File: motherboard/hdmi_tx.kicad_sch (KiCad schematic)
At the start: 49 parts, among them J8 HDMI_A, Q1 2SK3018W, Q2 2SK3018W, Q3 L2N7002WT1G, Q4 2SK3018W, Q5 2SK3018W, Q6 WNM6002-3/TR, Q7 WNM6002-3/TR, Q8 WNM6002-3/TR, Q9 WNM6002-3/TR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

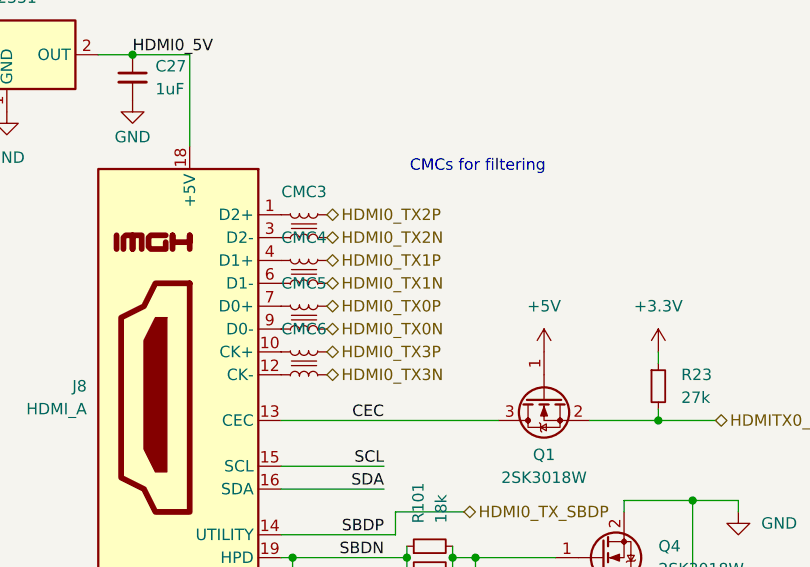
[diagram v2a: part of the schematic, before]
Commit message: 6 layer for better high speed signaling integrity
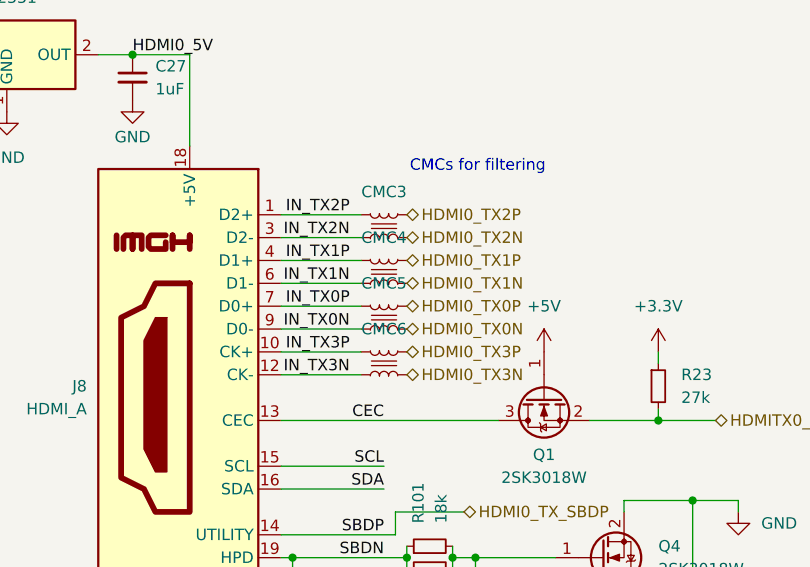
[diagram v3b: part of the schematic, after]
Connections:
- net IN_TX0N: now reaches CMC5.1, J8.9 (D0-)
- net IN_TX0P: now reaches CMC5.2, J8.7 (D0+)
- net IN_TX2P: now reaches CMC3.2, J8.1 (D2+)
- net IN_TX3P: now reaches CMC6.2, J8.10 (CK+)
- net IN_TX3N: now reaches CMC6.1, J8.12 (CK-)
- net IN_TX2N: now reaches CMC3.1, J8.3 (D2-)
- net IN_TX1P: now reaches CMC4.2, J8.4 (D1+)
- net IN_TX1N: now reaches CMC4.1, J8.6 (D1-)
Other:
- moved on the sheet: CMC3, CMC4, CMC5, CMC6
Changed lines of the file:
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@@
 	(wire
 		(pts
+			(xy 73.66 73.66) (xy 64.77 73.66)
+		)
+		(stroke
+			(width 0)
+			(type default)
+		)
+	)
+	(wire
+		(pts
+			(xy 73.66 76.2) (xy 64.77 76.2)
+		)
+		(stroke
+			(width 0)
+			(type default)
+		)
+	)
+	(wire
+		(pts
 			(xy 264.16 110.49) (xy 264.16 125.73)
 		)
@@
 	(wire
 		(pts
+			(xy 73.66 68.58) (xy 64.77 68.58)
+		)
+		(stroke
+			(width 0)
+			(type default)
+		)
+	)
+	(wire
+		(pts
+			(xy 73.66 63.5) (xy 64.77 63.5)
+		)
+		(stroke
+			(width 0)
+			(type default)
+		)
+	)
+	(wire
+		(pts
 			(xy 76.2 168.91) (xy 67.31 168.91)
 		)
@@
 	(wire
 		(pts
+			(xy 73.66 58.42) (xy 64.77 58.42)
+		)
+		(stroke
+			(width 0)
+			(type default)
+		)
+	)
+	(wire
+		(pts
 			(xy 207.01 49.53) (xy 207.01 50.8)
 		)
@@
 	(wire
 		(pts
+			(xy 73.66 66.04) (xy 64.77 66.04)
+		)
+		(stroke
+			(width 0)
+			(type default)
+		)
+	)
+	(wire
+		(pts
 			(xy 233.68 118.11) (xy 233.68 125.73)
 		)
@@
 	(wire
 		(pts
+			(xy 73.66 71.12) (xy 64.77 71.12)
+		)
+		(stroke
+			(width 0)
+			(type default)
+		)
+	)
+	(wire
+		(pts
 			(xy 267.97 134.62) (xy 267.97 132.08)
 		)
@@
 	(wire
 		(pts
+			(xy 73.66 60.96) (xy 64.77 60.96)
+		)
+		(stroke
+			(width 0)
+			(type default)
+		)
+	)
+	(wire
+		(pts
 			(xy 264.16 110.49) (xy 266.7 110.49)
 		)
@@
 		)
 	)
+	(label "IN_TX1P"
+		(at 72.39 63.5 180)
+		(fields_autoplaced yes)
+		(effects
+			(font
+				(size 1.27 1.27)
+			)
+			(justify right bottom)
+		)
+	)
 	(label "SBDN"
 		(at 110.49 173.99 180)
@@
 		)
 	)
+	(label "IN_TX1N"
+		(at 72.39 66.04 180)
+		(fields_autoplaced yes)
+		(effects
+			(font
+				(size 1.27 1.27)
+			)
+			(justify right bottom)
+		)
+	)
 	(label "SBDP"
 		(at 67.31 179.07 0)
@@
 		)
 	)
+	(label "IN_TX0N"
+		(at 72.39 71.12 180)
+		(fields_autoplaced yes)
+		(effects
+			(font
+				(size 1.27 1.27)
+			)
+			(justify right bottom)
+		)
+	)
 	(label "HDMI0_TX3N"
 		(at 156.21 149.86 180)
@@
 		)
 	)
+	(label "IN_TX3N"
+		(at 72.39 76.2 180)
+		(fields_autoplaced yes)
+		(effects
+			(font
+				(size 1.27 1.27)
+			)
+			(justify right bottom)
+		)
+	)
 	(label "HDMI0_TX2N"
 		(at 19.05 149.86 0)
@@
 		)
 	)
+	(label "IN_TX3P"
+		(at 72.39 73.66 180)
+		(fields_autoplaced yes)
+		(effects
+			(font
+				(size 1.27 1.27)
+			)
+			(justify right bottom)
+		)
+	)
 	(label "HDMI0_TX3P"
 		(at 181.61 123.19 0)
@@
 		)
 	)
+	(label "IN_TX2P"
+		(at 72.39 58.42 180)
+		(fields_autoplaced yes)
+		(effects
+			(font
+				(size 1.27 1.27)
+			)
+			(justify right bottom)
+		)
+	)
 	(label "HDMI0_TX2P"
 		(at 19.05 139.7 0)
@@
 		)
 	)
+	(label "IN_TX2N"
+		(at 72.39 60.96 180)
+		(fields_autoplaced yes)
+		(effects
+			(font
+				(size 1.27 1.27)
+			)
+			(justify right bottom)
+		)
+	)
+	(label "IN_TX0P"
+		(at 72.39 68.58 180)
+		(fields_autoplaced yes)
+		(effects
+			(font
+				(size 1.27 1.27)
+			)
+			(justify right bottom)
+		)
+	)
 	(label "HDMI0_TX1N"
 		(at 88.9 154.94 180)
@@
 	(hierarchical_label "HDMI0_TX1P"
 		(shape bidirectional)
-		(at 69.85 63.5 0)
+		(at 78.74 63.5 0)
 		(fields_autoplaced yes)
 		(effects
@@
 	(hierarchical_label "HDMI0_TX0N"
 		(shape bidirectional)
-		(at 69.85 71.12 0)
+		(at 78.74 71.12 0)
 		(fields_autoplaced yes)
 		(effects
@@
 	(hierarchical_label "HDMI0_TX0P"
 		(shape bidirectional)
-		(at 69.85 68.58 0)
+		(at 78.74 68.58 0)
 		(fields_autoplaced yes)
 		(effects
@@
 	(hierarchical_label "HDMI0_TX2N"
 		(shape bidirectional)
-		(at 69.85 60.96 0)
+		(at 78.74 60.96 0)
 		(fields_autoplaced yes)
 		(effects
@@
 	(hierarchical_label "HDMI0_TX3P"
 		(shape bidirectional)
-		(at 69.85 73.66 0)
+		(at 78.74 73.66 0)
 		(fields_autoplaced yes)
 		(effects
@@
 	(hierarchical_label "HDMI0_TX2P"
 		(shape bidirectional)
-		(at 69.85 58.42 0)
+		(at 78.74 58.42 0)
 		(fields_autoplaced yes)
 		(effects
@@
 	(hierarchical_label "HDMI0_TX3N"
 		(shape bidirectional)
-		(at 69.85 76.2 0)
+		(at 78.74 76.2 0)
 		(fields_autoplaced yes)
 		(effects
@@
 	(hierarchical_label "HDMI0_TX1N"
 		(shape bidirectional)
-		(at 69.85 66.04 0)
+		(at 78.74 66.04 0)
 		(fields_autoplaced yes)
 		(effects
@@
 	(symbol
 		(lib_id "library:ACM2012_Common_Mode_Choke")
-		(at 67.31 69.85 0)
+		(at 76.2 69.85 0)
 		(unit 1)
 		(exclude_from_sim no)
@@
 		(fields_autoplaced yes)
 		(property "Reference" "CMC5"
-			(at 67.31 66.04 0)
+			(at 76.2 66.04 0)
 			(effects
 				(font
@@
 		)
 		(property "Value" "ACM2012"
-			(at 71.501 73.025 0)
+			(at 80.391 73.025 0)
 			(effects
 				(font
@@
 		)
 		(property "Footprint" "ACM2012:FIL_ACM2012-900-2P-T001"
-			(at 65.278 78.232 0)
+			(at 74.168 78.232 0)
 			(effects
 				(font
@@
 		)
 		(property "Datasheet" "https://product.tdk.com/en/system/files?file=dam/doc/product/emc/emc/cmf_cmc/catalog/cmf_commercial_signal_acm2012_en.pdf"
-			(at 69.342 81.788 0)
+			(at 78.232 81.788 0)
 			(effects
 				(font
@@
 		)
 		(property "Description" "2 Line Common Mode Choke Surface Mount 90 Ohms @ 100 MHz 400mA DCR 190mOhm"
-			(at 67.818 75.946 0)
+			(at 76.708 75.946 0)
 			(effects
 				(font
@@
 	(symbol
 		(lib_id "library:ACM2012_Common_Mode_Choke")
-		(at 67.31 74.93 0)
+		(at 76.2 74.93 0)
 		(unit 1)
 		(exclude_from_sim no)
@@
 		(fields_autoplaced yes)
 		(property "Reference" "CMC6"
-			(at 67.31 71.12 0)
+			(at 76.2 71.12 0)
 			(effects
 				(font
@@
 		)
 		(property "Value" "ACM2012"
-			(at 71.501 78.105 0)
+			(at 80.391 78.105 0)
 			(effects
 				(font
@@
 		)
 		(property "Footprint" "ACM2012:FIL_ACM2012-900-2P-T001"
-			(at 65.278 83.312 0)
+			(at 74.168 83.312 0)
 			(effects
 				(font
@@
 		)
 		(property "Datasheet" "https://product.tdk.com/en/system/files?file=dam/doc/product/emc/emc/cmf_cmc/catalog/cmf_commercial_signal_acm2012_en.pdf"
-			(at 69.342 86.868 0)
+			(at 78.232 86.868 0)
 			(effects
 				(font
@@
 		)
 		(property "Description" "2 Line Common Mode Choke Surface Mount 90 Ohms @ 100 MHz 400mA DCR 190mOhm"
-			(at 67.818 81.026 0)
+			(at 76.708 81.026 0)
 			(effects
 				(font
@@
 	(symbol
 		(lib_id "library:ACM2012_Common_Mode_Choke")
-		(at 67.31 64.77 0)
+		(at 76.2 64.77 0)
 		(unit 1)
 		(exclude_from_sim no)
@@
 		(fields_autoplaced yes)
 		(property "Reference" "CMC4"
-			(at 67.31 60.96 0)
+			(at 76.2 60.96 0)
 			(effects
 				(font
@@
 		)
 		(property "Value" "ACM2012"
-			(at 71.501 67.945 0)
+			(at 80.391 67.945 0)
 			(effects
 				(font
@@
 		)
 		(property "Footprint" "ACM2012:FIL_ACM2012-900-2P-T001"
-			(at 65.278 73.152 0)
+			(at 74.168 73.152 0)
 			(effects
 				(font
@@
 		)
 		(property "Datasheet" "https://product.tdk.com/en/system/files?file=dam/doc/product/emc/emc/cmf_cmc/catalog/cmf_commercial_signal_acm2012_en.pdf"
-			(at 69.342 76.708 0)
+			(at 78.232 76.708 0)
 			(effects
 				(font
@@
 		)
 		(property "Description" "2 Line Common Mode Choke Surface Mount 90 Ohms @ 100 MHz 400mA DCR 190mOhm"
-			(at 67.818 70.866 0)
+			(at 76.708 70.866 0)
 			(effects
 				(font
@@
 	(symbol
 		(lib_id "library:ACM2012_Common_Mode_Choke")
-		(at 67.31 59.69 0)
+		(at 76.2 59.69 0)
 		(unit 1)
 		(exclude_from_sim no)
@@
 		(fields_autoplaced yes)
 		(property "Reference" "CMC3"
-			(at 67.31 55.88 0)
+			(at 76.2 55.88 0)
 			(effects
 				(font
@@
 		)
 		(property "Value" "ACM2012"
-			(at 71.501 62.865 0)
+			(at 80.391 62.865 0)
 			(effects
 				(font
@@
 		)
 		(property "Footprint" "ACM2012:FIL_ACM2012-900-2P-T001"
-			(at 65.278 68.072 0)
+			(at 74.168 68.072 0)
 			(effects
 				(font
@@
 		)
 		(property "Datasheet" "https://product.tdk.com/en/system/files?file=dam/doc/product/emc/emc/cmf_cmc/catalog/cmf_commercial_signal_acm2012_en.pdf"
-			(at 69.342 71.628 0)
+			(at 78.232 71.628 0)
 			(effects
 				(font
@@
 		)
 		(property "Description" "2 Line Common Mode Choke Surface Mount 90 Ohms @ 100 MHz 400mA DCR 190mOhm"
-			(at 67.818 65.786 0)
+			(at 76.708 65.786 0)
 			(effects
 				(font

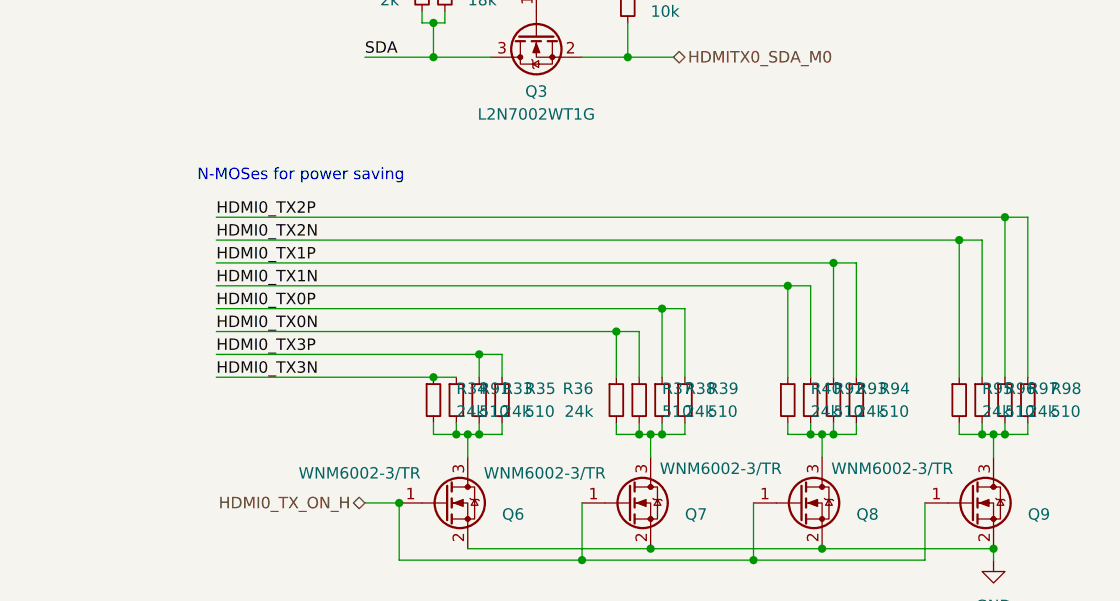
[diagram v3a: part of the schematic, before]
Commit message: rerouting high speed traces
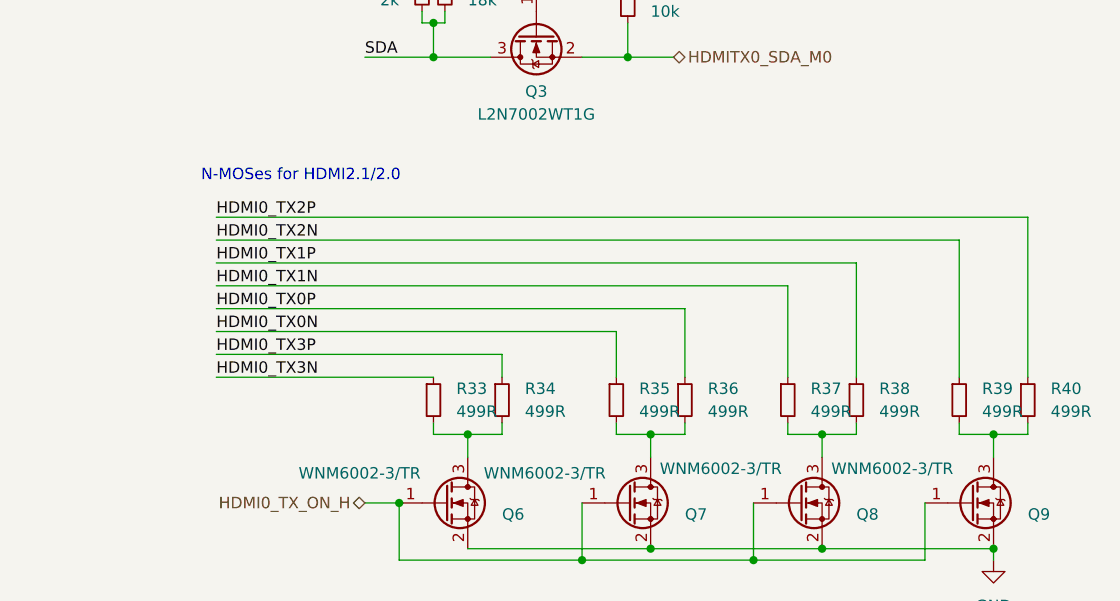
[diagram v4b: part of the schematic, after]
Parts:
- removed R91, R92, R94, R96, R98: 510, Resistor_SMD:R_0402_1005Metric, symbol Device:R_Small
- removed R93, R95, R97: 24k, Resistor_SMD:R_0402_1005Metric, symbol Device:R_Small
- R33, R34, R36, R38, R40: value 24k -> 499R
- R35, R37, R39: value 510 -> 499R
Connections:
- net HDMI0_TX0N: now also R35.1; no longer R36.1, R37.1
- net HDMI0_TX0P: now also R36.1; no longer R38.1, R39.1
- net HDMI0_TX1N: now also R37.1; no longer R40.1
- net HDMI0_TX1P: now also R38.1
- net HDMI0_TX2N: now also R39.1
- net HDMI0_TX2P: now also R40.1
- net HDMI0_TX3N: now also R33.1; no longer R34.1
- net HDMI0_TX3P: now also R34.1; no longer R33.1, R35.1
- net at Q9.3 (D): now also R39.2, R40.2
- net at Q6.3 (D), R33.2, R34.2: no longer R35.2
- net at Q8.3 (D): now also R37.2, R38.2; no longer R40.2
- new net: Q7.3 (D), R35.2, R36.2
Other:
- note added: "N-MOSes for HDMI2.1/2.0"
- note removed: "N-MOSes for power saving"
